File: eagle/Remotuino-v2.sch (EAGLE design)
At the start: 41 parts, among them Q1 16MHz, Q2 BSS138, Q3 BSS138, U1 ATMEGA324P, U2 MIC5209-3.3YS, U3 XBEE

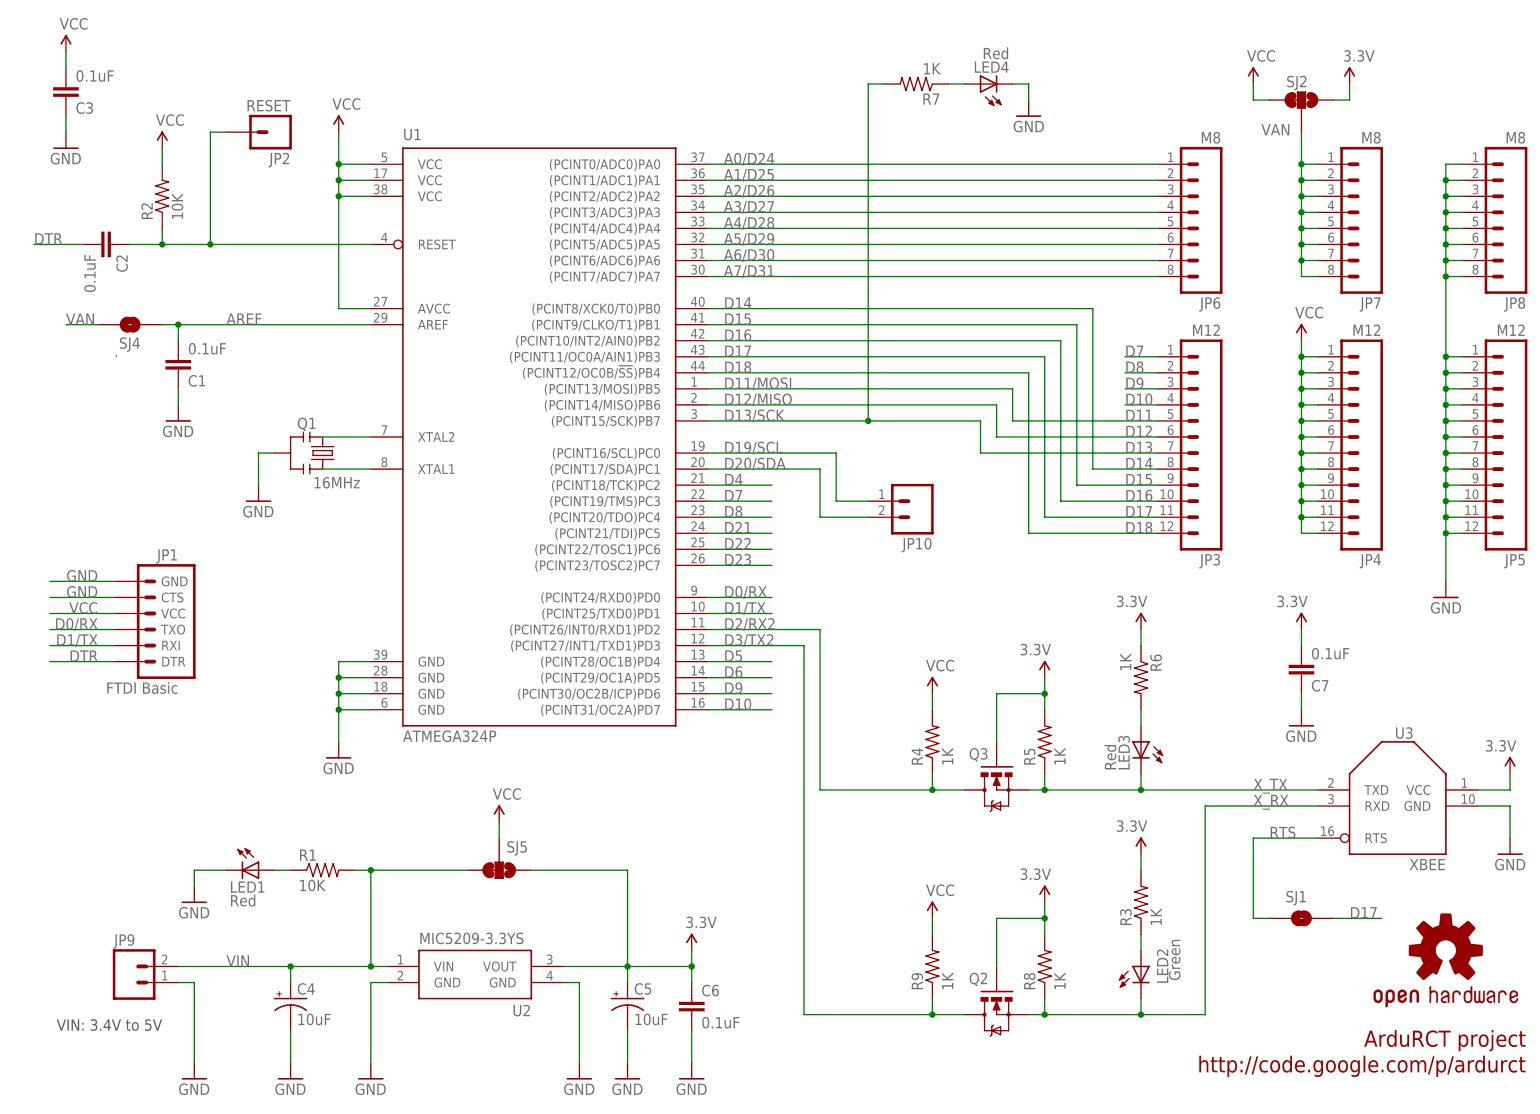
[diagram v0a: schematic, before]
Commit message: 
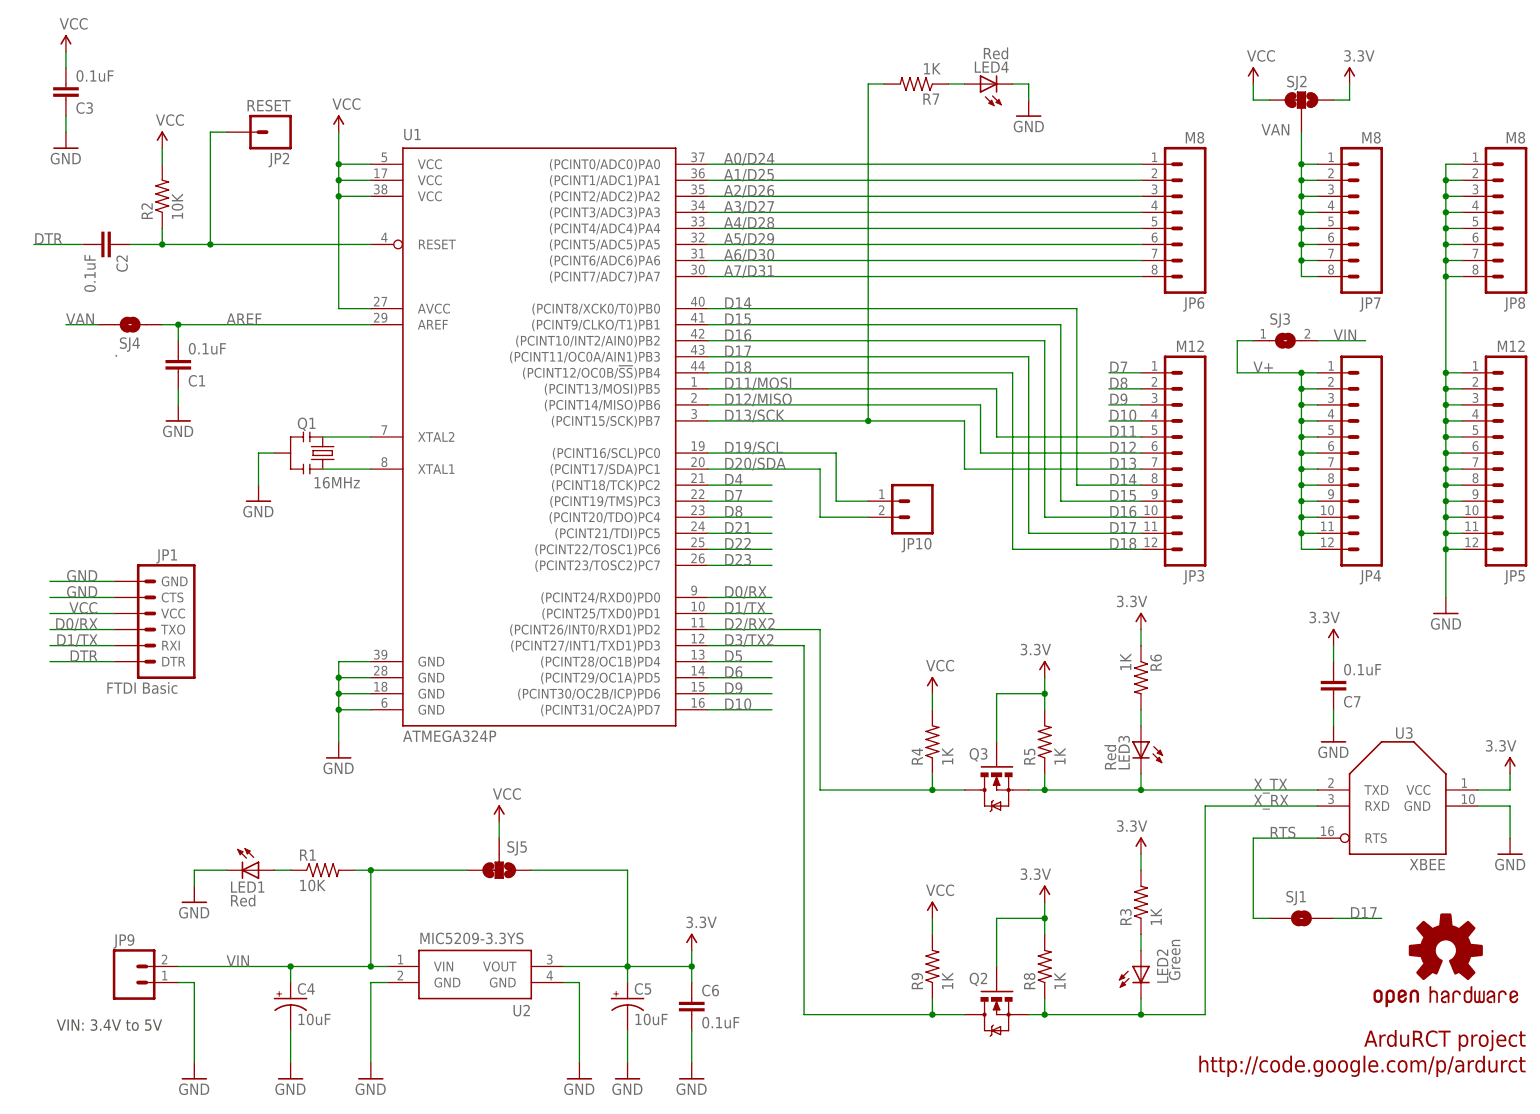
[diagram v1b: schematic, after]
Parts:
- added SJ3: (no value), wibauxl:SJ
- JP4: value M12 -> M12PTH
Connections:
- new net V+: JP4.1, JP4.10, JP4.11, JP4.12, JP4.2, JP4.3, JP4.4, JP4.5, JP4.6, JP4.7, JP4.8, JP4.9, SJ3.1
- net VCC: no longer JP4.1, JP4.10, JP4.11, JP4.12, JP4.2, JP4.3, JP4.4, JP4.5, JP4.6, JP4.7, JP4.8, JP4.9
- net VIN: now also SJ3.2
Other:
- moved on the sheet: C7, JP3, JP4, JP5, JP6
